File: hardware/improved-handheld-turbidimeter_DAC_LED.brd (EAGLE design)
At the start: 23 x 17.8 mm, 14 parts

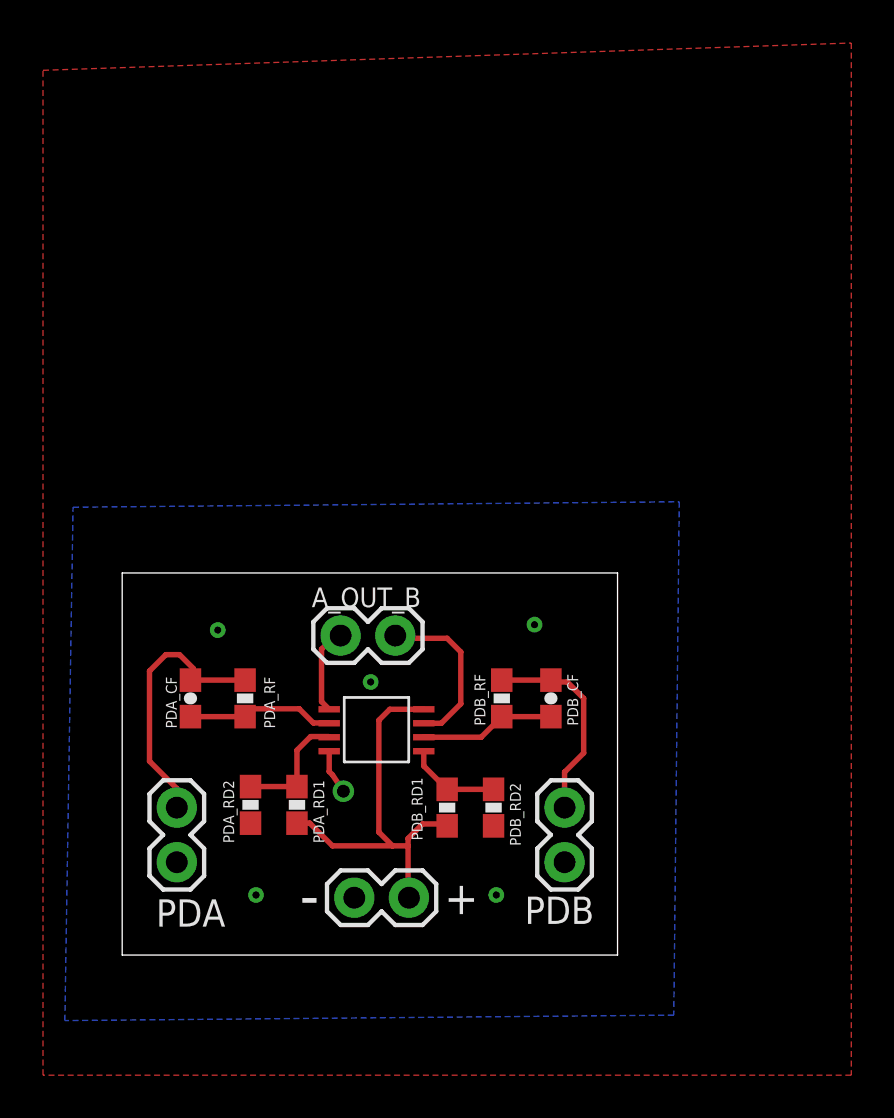
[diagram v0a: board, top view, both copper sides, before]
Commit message: new and updated component boards
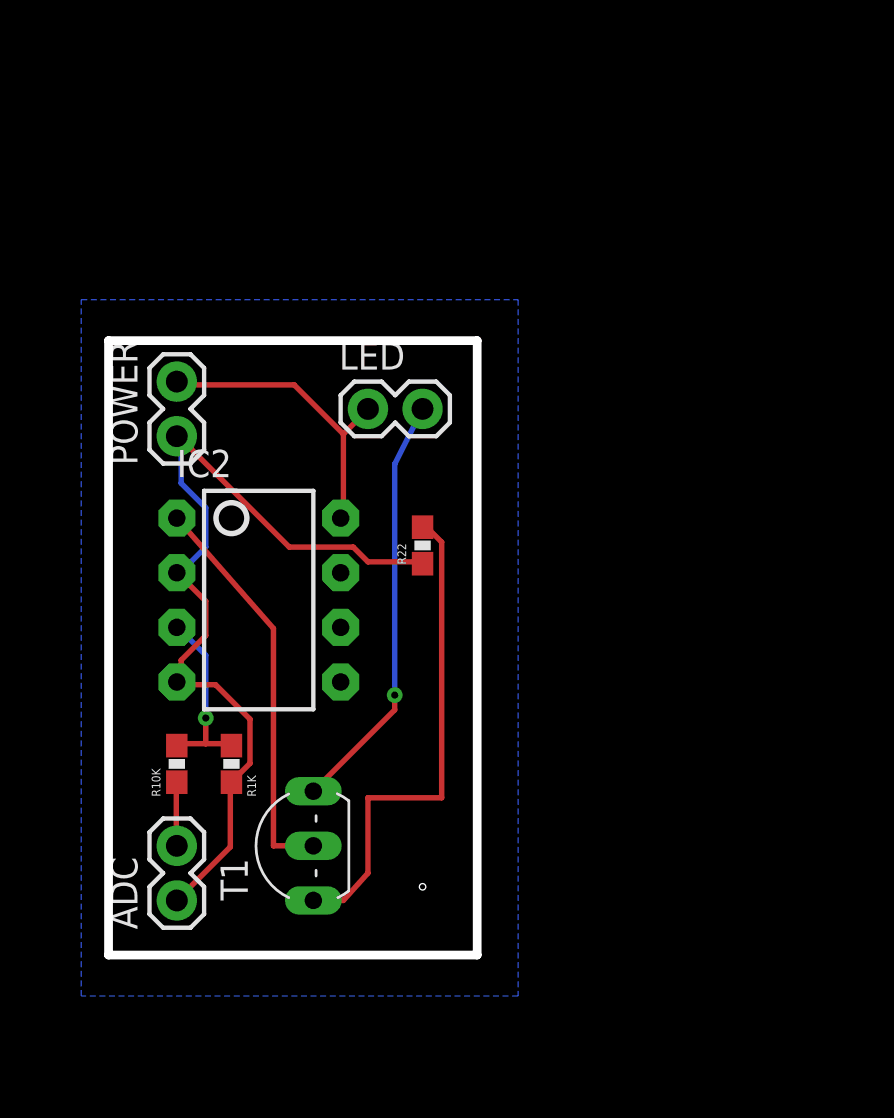
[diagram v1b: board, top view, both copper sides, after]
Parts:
- removed A_OUT_B, JP3, PDA, PDB: (no value), SparkFun-Connectors:1X02
- removed FRAME1: FRAME-LETTER, SparkFun-Aesthetics:CREATIVE_COMMONS
- removed PDA_CF, PDB_CF: (no value), SparkFun-Passives:0603-CAP
- removed PDA_RD1, PDA_RD2, PDA_RF, PDB_RD1, PDB_RD2, PDB_RF: (no value), SparkFun-Passives:0603-RES
- removed U$2: ADA4528-2, awqua_eagle_library:ADA4528-2
- added ADC, LED, POWER: (no value), SparkFun-Connectors:1X02
- added IC2: LM358, SparkFun-AnalogIC:DIP08
- added R10K, R1K, R22: (no value), SparkFun-Passives:0603-RES
- added T1: 2N2222, adafruit:TO92-EBC-OVAL
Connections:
- removed net GND: JP3.2, PDA.2, PDA_RD2.1, PDB.1, PDB_RD2.1, U$2.P$4
- removed net N$4: PDB_CF.1, PDB_RF.2, U$2.P$6
- removed net OUTA: A_OUT_B.1, U$2.P$1
- removed net OUTB: A_OUT_B.2, U$2.P$7
- removed net VCC: JP3.1, PDA_RD1.1, PDB_RD1.1, U$2.P$8
- new net 3.3V: IC2.8, LED.1, POWER.2
- new net AGND: ADC.1, IC2.2, IC2.4, POWER.1, R1K.1, R22.1
- net N$1: now also IC2.1, T1.B; no longer PDA.1, PDA_CF.2, PDA_RF.1
- net N$2: now also LED.2, T1.C; no longer PDA_CF.1, PDA_RF.2, U$2.P$2
- net N$3: now also R22.2, T1.E; no longer PDB.2, PDB_CF.2, PDB_RF.1
- net N$5: now also ADC.2, R10K.2; no longer PDA_RD1.2, PDA_RD2.2, U$2.P$3
- net N$6: now also IC2.3, R10K.1, R1K.2; no longer PDB_RD1.2, PDB_RD2.2, U$2.P$5
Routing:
- net AGND: track 0.00 -> 41.7 mm
- net VCC: track 18.9 -> 0.00 mm
- net 3.3V: track 0.00 -> 14.4 mm
- net N$3: track 9.61 -> 23.1 mm
- net N$2: track 6.88 -> 19.7 mm, vias 0 -> 1
- net OUTB: track 7.87 -> 0.00 mm
- net N$4: track 6.82 -> 0.00 mm
- net N$1: track 12.6 -> 18.8 mm
- net N$6: track 4.38 -> 8.60 mm, vias 0 -> 1
- net OUTA: track 4.09 -> 0.00 mm
- net N$5: track 5.62 -> 2.97 mm
- net GND: track 2.08 -> 0.00 mm, vias 1 -> 0
- added copper zone on layer 16, net AGND
- removed copper zone on layer 1, net GND
- removed copper zone on layer 16, net GND
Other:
- board size 23 x 17.8 mm -> 17.1 x 28.6 mm
- board text added: "AWQUA DAC-LED board v1.0 10/28/2016"
- board text removed: "+"
- board text removed: "-"
- board text removed: "AWQUA TIA Board v1.1 2016/10/27"
- board text removed: "Chris Kelley"
